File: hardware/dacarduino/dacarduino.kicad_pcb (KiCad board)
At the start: 2 copper layers, 98 x 98 mm, 78 parts, among them J1 Conn_01x03_Male, J10 Conn_01x02, J11 GATE IN, J12 GATE IN, J13 GATE IN, J14 GATE IN, J15 CV IN, J16 CV IN, J17 CV IN, J18 CV IN, J2 Conn_01x03_Male, J3 Molex 2 pin, J4 Molex 2 pin, J5 Molex 2 pin, J6 Molex 2 pin, J7 VCC, J8 EURO_PWR_2x5, J9 Conn_01x04, Q1 2N3904, Q2 2N3904, Q3 2N3904, Q4 2N3904, Q5 2N3904, Q6 2N3904, U1 MCP4922, U2 TL072, U3 REF02CP+

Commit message: Added hack area
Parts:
- added REF**: SolderWirePad_1x01_Drill0.8mm, Connector_Wire:SolderWirePad_1x01_Drill0.8mm, F.Cu at (106.7, 81.3)
- added REF**: SolderWirePad_1x01_Drill0.8mm, Connector_Wire:SolderWirePad_1x01_Drill0.8mm, F.Cu at (116.8, 88.9)
- added REF**: SolderWirePad_1x01_Drill0.8mm, Connector_Wire:SolderWirePad_1x01_Drill0.8mm, F.Cu at (94.0, 86.4)
- added REF**: SolderWirePad_1x01_Drill0.8mm, Connector_Wire:SolderWirePad_1x01_Drill0.8mm, F.Cu at (116.8, 101.6)
- added REF**: SolderWirePad_1x01_Drill0.8mm, Connector_Wire:SolderWirePad_1x01_Drill0.8mm, F.Cu at (116.8, 91.4)
- added REF**: SolderWirePad_1x01_Drill0.8mm, Connector_Wire:SolderWirePad_1x01_Drill0.8mm, F.Cu at (116.8, 99.1)
- added REF**: SolderWirePad_1x01_Drill0.8mm, Connector_Wire:SolderWirePad_1x01_Drill0.8mm, F.Cu at (116.8, 94.0)
- added REF**: SolderWirePad_1x01_Drill0.8mm, Connector_Wire:SolderWirePad_1x01_Drill0.8mm, F.Cu at (116.8, 96.5)
- added REF**: SolderWirePad_1x01_Drill0.8mm, Connector_Wire:SolderWirePad_1x01_Drill0.8mm, F.Cu at (101.6, 78.7)
- added REF**: SolderWirePad_1x01_Drill0.8mm, Connector_Wire:SolderWirePad_1x01_Drill0.8mm, F.Cu at (101.6, 81.3)
- added REF**: SolderWirePad_1x01_Drill0.8mm, Connector_Wire:SolderWirePad_1x01_Drill0.8mm, F.Cu at (101.6, 83.8)
- added REF**: SolderWirePad_1x01_Drill0.8mm, Connector_Wire:SolderWirePad_1x01_Drill0.8mm, F.Cu at (91.4, 78.7)
- added REF**: SolderWirePad_1x01_Drill0.8mm, Connector_Wire:SolderWirePad_1x01_Drill0.8mm, F.Cu at (104.1, 81.3)
- added REF**: SolderWirePad_1x01_Drill0.8mm, Connector_Wire:SolderWirePad_1x01_Drill0.8mm, F.Cu at (96.5, 78.7)
- added REF**: SolderWirePad_1x01_Drill0.8mm, Connector_Wire:SolderWirePad_1x01_Drill0.8mm, F.Cu at (99.1, 78.7)
- added REF**: SolderWirePad_1x01_Drill0.8mm, Connector_Wire:SolderWirePad_1x01_Drill0.8mm, F.Cu at (94.0, 78.7)
- added REF**: SolderWirePad_1x01_Drill0.8mm, Connector_Wire:SolderWirePad_1x01_Drill0.8mm, F.Cu at (91.4, 81.3)
- added REF**: SolderWirePad_1x01_Drill0.8mm, Connector_Wire:SolderWirePad_1x01_Drill0.8mm, F.Cu at (96.5, 81.3)
- added REF**: SolderWirePad_1x01_Drill0.8mm, Connector_Wire:SolderWirePad_1x01_Drill0.8mm, F.Cu at (94.0, 81.3)
- added REF**: SolderWirePad_1x01_Drill0.8mm, Connector_Wire:SolderWirePad_1x01_Drill0.8mm, F.Cu at (99.1, 81.3)
- added REF**: SolderWirePad_1x01_Drill0.8mm, Connector_Wire:SolderWirePad_1x01_Drill0.8mm, F.Cu at (94.0, 83.8)
- added REF**: SolderWirePad_1x01_Drill0.8mm, Connector_Wire:SolderWirePad_1x01_Drill0.8mm, F.Cu at (99.1, 83.8)
- added REF**: SolderWirePad_1x01_Drill0.8mm, Connector_Wire:SolderWirePad_1x01_Drill0.8mm, F.Cu at (96.5, 83.8)
- added REF**: SolderWirePad_1x01_Drill0.8mm, Connector_Wire:SolderWirePad_1x01_Drill0.8mm, F.Cu at (104.1, 83.8)
- added REF**: SolderWirePad_1x01_Drill0.8mm, Connector_Wire:SolderWirePad_1x01_Drill0.8mm, F.Cu at (91.4, 83.8)
- added REF**: SolderWirePad_1x01_Drill0.8mm, Connector_Wire:SolderWirePad_1x01_Drill0.8mm, F.Cu at (114.3, 99.1)
- added REF**: SolderWirePad_1x01_Drill0.8mm, Connector_Wire:SolderWirePad_1x01_Drill0.8mm, F.Cu at (114.3, 101.6)
- added REF**: SolderWirePad_1x01_Drill0.8mm, Connector_Wire:SolderWirePad_1x01_Drill0.8mm, F.Cu at (114.3, 94.0)
- added REF**: SolderWirePad_1x01_Drill0.8mm, Connector_Wire:SolderWirePad_1x01_Drill0.8mm, F.Cu at (114.3, 96.5)
- added REF**: SolderWirePad_1x01_Drill0.8mm, Connector_Wire:SolderWirePad_1x01_Drill0.8mm, F.Cu at (114.3, 91.4)
- added REF**: SolderWirePad_1x01_Drill0.8mm, Connector_Wire:SolderWirePad_1x01_Drill0.8mm, F.Cu at (114.3, 88.9)
- added REF**: SolderWirePad_1x01_Drill0.8mm, Connector_Wire:SolderWirePad_1x01_Drill0.8mm, F.Cu at (101.6, 104.1)
- added REF**: SolderWirePad_1x01_Drill0.8mm, Connector_Wire:SolderWirePad_1x01_Drill0.8mm, F.Cu at (104.1, 104.1)
- added REF**: SolderWirePad_1x01_Drill0.8mm, Connector_Wire:SolderWirePad_1x01_Drill0.8mm, F.Cu at (99.1, 104.1)
- added REF**: SolderWirePad_1x01_Drill0.8mm, Connector_Wire:SolderWirePad_1x01_Drill0.8mm, F.Cu at (106.7, 83.8)
- added REF**: SolderWirePad_1x01_Drill0.8mm, Connector_Wire:SolderWirePad_1x01_Drill0.8mm, F.Cu at (91.4, 104.1)
- added REF**: SolderWirePad_1x01_Drill0.8mm, Connector_Wire:SolderWirePad_1x01_Drill0.8mm, F.Cu at (94.0, 104.1)
- added REF**: SolderWirePad_1x01_Drill0.8mm, Connector_Wire:SolderWirePad_1x01_Drill0.8mm, F.Cu at (106.7, 104.1)
- added REF**: SolderWirePad_1x01_Drill0.8mm, Connector_Wire:SolderWirePad_1x01_Drill0.8mm, F.Cu at (109.2, 104.1)
- added REF**: SolderWirePad_1x01_Drill0.8mm, Connector_Wire:SolderWirePad_1x01_Drill0.8mm, F.Cu at (96.5, 104.1)
- added REF**: SolderWirePad_1x01_Drill0.8mm, Connector_Wire:SolderWirePad_1x01_Drill0.8mm, F.Cu at (99.1, 101.6)
- added REF**: SolderWirePad_1x01_Drill0.8mm, Connector_Wire:SolderWirePad_1x01_Drill0.8mm, F.Cu at (104.1, 101.6)
- added REF**: SolderWirePad_1x01_Drill0.8mm, Connector_Wire:SolderWirePad_1x01_Drill0.8mm, F.Cu at (91.4, 101.6)
- added REF**: SolderWirePad_1x01_Drill0.8mm, Connector_Wire:SolderWirePad_1x01_Drill0.8mm, F.Cu at (106.7, 101.6)
- added REF**: SolderWirePad_1x01_Drill0.8mm, Connector_Wire:SolderWirePad_1x01_Drill0.8mm, F.Cu at (109.2, 101.6)
- added REF**: SolderWirePad_1x01_Drill0.8mm, Connector_Wire:SolderWirePad_1x01_Drill0.8mm, F.Cu at (109.2, 83.8)
- added REF**: SolderWirePad_1x01_Drill0.8mm, Connector_Wire:SolderWirePad_1x01_Drill0.8mm, F.Cu at (96.5, 101.6)
- added REF**: SolderWirePad_1x01_Drill0.8mm, Connector_Wire:SolderWirePad_1x01_Drill0.8mm, F.Cu at (94.0, 101.6)
- added REF**: SolderWirePad_1x01_Drill0.8mm, Connector_Wire:SolderWirePad_1x01_Drill0.8mm, F.Cu at (101.6, 101.6)
- added REF**: SolderWirePad_1x01_Drill0.8mm, Connector_Wire:SolderWirePad_1x01_Drill0.8mm, F.Cu at (104.1, 99.1)
- added REF**: SolderWirePad_1x01_Drill0.8mm, Connector_Wire:SolderWirePad_1x01_Drill0.8mm, F.Cu at (106.7, 99.1)
- added REF**: SolderWirePad_1x01_Drill0.8mm, Connector_Wire:SolderWirePad_1x01_Drill0.8mm, F.Cu at (94.0, 99.1)
- added REF**: SolderWirePad_1x01_Drill0.8mm, Connector_Wire:SolderWirePad_1x01_Drill0.8mm, F.Cu at (91.4, 99.1)
- added REF**: SolderWirePad_1x01_Drill0.8mm, Connector_Wire:SolderWirePad_1x01_Drill0.8mm, F.Cu at (101.6, 99.1)
- added REF**: SolderWirePad_1x01_Drill0.8mm, Connector_Wire:SolderWirePad_1x01_Drill0.8mm, F.Cu at (99.1, 99.1)
- added REF**: SolderWirePad_1x01_Drill0.8mm, Connector_Wire:SolderWirePad_1x01_Drill0.8mm, F.Cu at (96.5, 99.1)
- added REF**: SolderWirePad_1x01_Drill0.8mm, Connector_Wire:SolderWirePad_1x01_Drill0.8mm, F.Cu at (109.2, 81.3)
- added REF**: SolderWirePad_1x01_Drill0.8mm, Connector_Wire:SolderWirePad_1x01_Drill0.8mm, F.Cu at (109.2, 99.1)
- added REF**: SolderWirePad_1x01_Drill0.8mm, Connector_Wire:SolderWirePad_1x01_Drill0.8mm, F.Cu at (101.6, 96.5)
- added REF**: SolderWirePad_1x01_Drill0.8mm, Connector_Wire:SolderWirePad_1x01_Drill0.8mm, F.Cu at (109.2, 96.5)
- added REF**: SolderWirePad_1x01_Drill0.8mm, Connector_Wire:SolderWirePad_1x01_Drill0.8mm, F.Cu at (96.5, 96.5)
- added REF**: SolderWirePad_1x01_Drill0.8mm, Connector_Wire:SolderWirePad_1x01_Drill0.8mm, F.Cu at (91.4, 96.5)
- added REF**: SolderWirePad_1x01_Drill0.8mm, Connector_Wire:SolderWirePad_1x01_Drill0.8mm, F.Cu at (104.1, 96.5)
- added REF**: SolderWirePad_1x01_Drill0.8mm, Connector_Wire:SolderWirePad_1x01_Drill0.8mm, F.Cu at (106.7, 96.5)
- added REF**: SolderWirePad_1x01_Drill0.8mm, Connector_Wire:SolderWirePad_1x01_Drill0.8mm, F.Cu at (99.1, 96.5)
- added REF**: SolderWirePad_1x01_Drill0.8mm, Connector_Wire:SolderWirePad_1x01_Drill0.8mm, F.Cu at (94.0, 96.5)
- added REF**: SolderWirePad_1x01_Drill0.8mm, Connector_Wire:SolderWirePad_1x01_Drill0.8mm, F.Cu at (94.0, 94.0)
- added REF**: SolderWirePad_1x01_Drill0.8mm, Connector_Wire:SolderWirePad_1x01_Drill0.8mm, F.Cu at (109.2, 78.7)
- added REF**: SolderWirePad_1x01_Drill0.8mm, Connector_Wire:SolderWirePad_1x01_Drill0.8mm, F.Cu at (96.5, 94.0)
- added REF**: SolderWirePad_1x01_Drill0.8mm, Connector_Wire:SolderWirePad_1x01_Drill0.8mm, F.Cu at (109.2, 94.0)
- added REF**: SolderWirePad_1x01_Drill0.8mm, Connector_Wire:SolderWirePad_1x01_Drill0.8mm, F.Cu at (101.6, 94.0)
- added REF**: SolderWirePad_1x01_Drill0.8mm, Connector_Wire:SolderWirePad_1x01_Drill0.8mm, F.Cu at (91.4, 94.0)
- added REF**: SolderWirePad_1x01_Drill0.8mm, Connector_Wire:SolderWirePad_1x01_Drill0.8mm, F.Cu at (106.7, 94.0)
- added REF**: SolderWirePad_1x01_Drill0.8mm, Connector_Wire:SolderWirePad_1x01_Drill0.8mm, F.Cu at (99.1, 94.0)
- added REF**: SolderWirePad_1x01_Drill0.8mm, Connector_Wire:SolderWirePad_1x01_Drill0.8mm, F.Cu at (104.1, 94.0)
- added REF**: SolderWirePad_1x01_Drill0.8mm, Connector_Wire:SolderWirePad_1x01_Drill0.8mm, F.Cu at (106.7, 91.4)
- added REF**: SolderWirePad_1x01_Drill0.8mm, Connector_Wire:SolderWirePad_1x01_Drill0.8mm, F.Cu at (91.4, 91.4)
- added REF**: SolderWirePad_1x01_Drill0.8mm, Connector_Wire:SolderWirePad_1x01_Drill0.8mm, F.Cu at (104.1, 91.4)
- added REF**: SolderWirePad_1x01_Drill0.8mm, Connector_Wire:SolderWirePad_1x01_Drill0.8mm, F.Cu at (106.7, 78.7)
- added REF**: SolderWirePad_1x01_Drill0.8mm, Connector_Wire:SolderWirePad_1x01_Drill0.8mm, F.Cu at (94.0, 91.4)
- added REF**: SolderWirePad_1x01_Drill0.8mm, Connector_Wire:SolderWirePad_1x01_Drill0.8mm, F.Cu at (109.2, 91.4)
- added REF**: SolderWirePad_1x01_Drill0.8mm, Connector_Wire:SolderWirePad_1x01_Drill0.8mm, F.Cu at (96.5, 91.4)
- added REF**: SolderWirePad_1x01_Drill0.8mm, Connector_Wire:SolderWirePad_1x01_Drill0.8mm, F.Cu at (99.1, 91.4)
- added REF**: SolderWirePad_1x01_Drill0.8mm, Connector_Wire:SolderWirePad_1x01_Drill0.8mm, F.Cu at (101.6, 91.4)
- added REF**: SolderWirePad_1x01_Drill0.8mm, Connector_Wire:SolderWirePad_1x01_Drill0.8mm, F.Cu at (94.0, 88.9)
- added REF**: SolderWirePad_1x01_Drill0.8mm, Connector_Wire:SolderWirePad_1x01_Drill0.8mm, F.Cu at (106.7, 88.9)
- added REF**: SolderWirePad_1x01_Drill0.8mm, Connector_Wire:SolderWirePad_1x01_Drill0.8mm, F.Cu at (99.1, 88.9)
- added REF**: SolderWirePad_1x01_Drill0.8mm, Connector_Wire:SolderWirePad_1x01_Drill0.8mm, F.Cu at (109.2, 88.9)
- added REF**: SolderWirePad_1x01_Drill0.8mm, Connector_Wire:SolderWirePad_1x01_Drill0.8mm, F.Cu at (96.5, 88.9)
- added REF**: SolderWirePad_1x01_Drill0.8mm, Connector_Wire:SolderWirePad_1x01_Drill0.8mm, F.Cu at (104.1, 78.7)
- added REF**: SolderWirePad_1x01_Drill0.8mm, Connector_Wire:SolderWirePad_1x01_Drill0.8mm, F.Cu at (101.6, 88.9)
- added REF**: SolderWirePad_1x01_Drill0.8mm, Connector_Wire:SolderWirePad_1x01_Drill0.8mm, F.Cu at (91.4, 88.9)
- added REF**: SolderWirePad_1x01_Drill0.8mm, Connector_Wire:SolderWirePad_1x01_Drill0.8mm, F.Cu at (104.1, 88.9)
- added REF**: SolderWirePad_1x01_Drill0.8mm, Connector_Wire:SolderWirePad_1x01_Drill0.8mm, F.Cu at (91.4, 86.4)
- added REF**: SolderWirePad_1x01_Drill0.8mm, Connector_Wire:SolderWirePad_1x01_Drill0.8mm, F.Cu at (109.2, 86.4)
- added REF**: SolderWirePad_1x01_Drill0.8mm, Connector_Wire:SolderWirePad_1x01_Drill0.8mm, F.Cu at (106.7, 86.4)
- added REF**: SolderWirePad_1x01_Drill0.8mm, Connector_Wire:SolderWirePad_1x01_Drill0.8mm, F.Cu at (104.1, 86.4)
- added REF**: SolderWirePad_1x01_Drill0.8mm, Connector_Wire:SolderWirePad_1x01_Drill0.8mm, F.Cu at (101.6, 86.4)
- added REF**: SolderWirePad_1x01_Drill0.8mm, Connector_Wire:SolderWirePad_1x01_Drill0.8mm, F.Cu at (99.1, 86.4)
- added REF**: SolderWirePad_1x01_Drill0.8mm, Connector_Wire:SolderWirePad_1x01_Drill0.8mm, F.Cu at (96.5, 86.4)
- moved R12 6.74 mm to (120.7, 79.4)
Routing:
- net /Arduino/DAC_CS: track 63.8 -> 60.6 mm
- net VCC: track 264.7 -> 266.1 mm
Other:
- board text added: "GND"
- board text added: "Hack me here"
- board text added: "VCC"

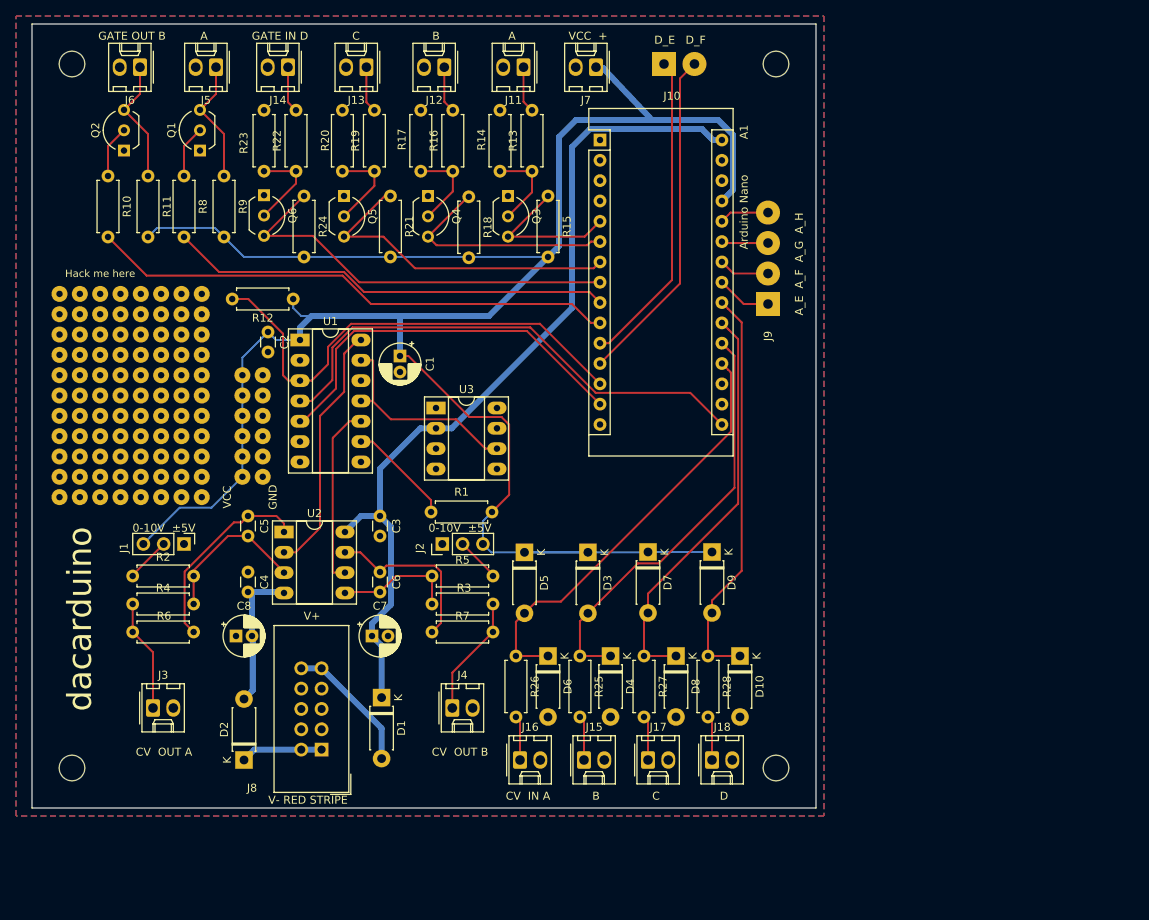
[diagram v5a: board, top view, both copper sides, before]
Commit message: Add multiplexer option
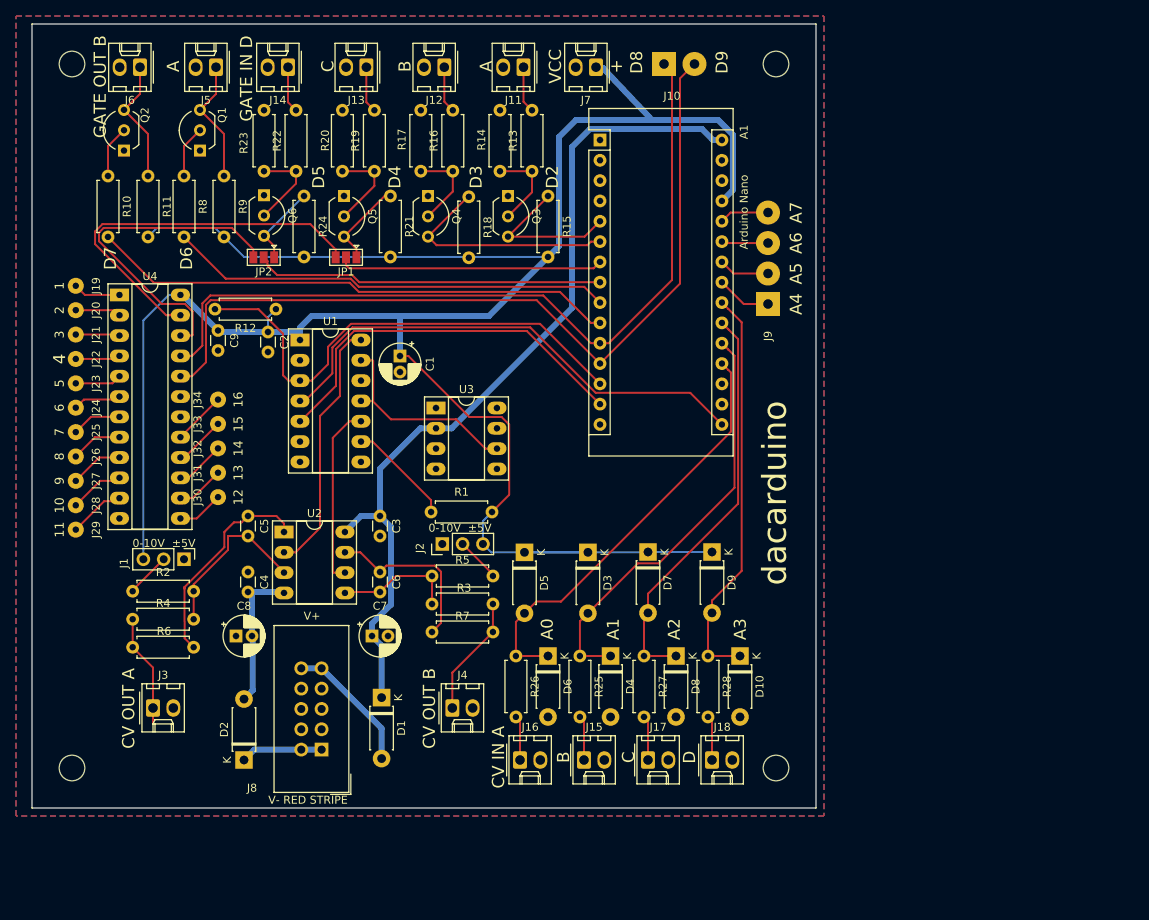
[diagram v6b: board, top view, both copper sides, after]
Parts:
- removed REF** (x100): SolderWirePad_1x01_Drill0.8mm, Connector_Wire:SolderWirePad_1x01_Drill0.8mm
- added C9: 0.1uF, Capacitor_THT:C_Disc_D3.0mm_W1.6mm_P2.50mm, F.Cu at (111.3, 83.3)
- added J19: Conn_01x01, Connector_Wire:SolderWirePad_1x01_Drill0.8mm, F.Cu at (93.5, 77.7)
- added J20: Conn_01x01, Connector_Wire:SolderWirePad_1x01_Drill0.8mm, F.Cu at (93.5, 80.8)
- added J21: Conn_01x01, Connector_Wire:SolderWirePad_1x01_Drill0.8mm, F.Cu at (93.5, 83.8)
- added J22: Conn_01x01, Connector_Wire:SolderWirePad_1x01_Drill0.8mm, F.Cu at (93.5, 86.9)
- added J23: Conn_01x01, Connector_Wire:SolderWirePad_1x01_Drill0.8mm, F.Cu at (93.5, 89.9)
- added J24: Conn_01x01, Connector_Wire:SolderWirePad_1x01_Drill0.8mm, F.Cu at (93.5, 93.0)
- added J25: Conn_01x01, Connector_Wire:SolderWirePad_1x01_Drill0.8mm, F.Cu at (93.5, 96.0)
- added J26: Conn_01x01, Connector_Wire:SolderWirePad_1x01_Drill0.8mm, F.Cu at (93.5, 99.1)
- added J27: Conn_01x01, Connector_Wire:SolderWirePad_1x01_Drill0.8mm, F.Cu at (93.5, 102.1)
- added J28: Conn_01x01, Connector_Wire:SolderWirePad_1x01_Drill0.8mm, F.Cu at (93.5, 105.2)
- added J29: Conn_01x01, Connector_Wire:SolderWirePad_1x01_Drill0.8mm, F.Cu at (93.5, 108.2)
- added J30: Conn_01x01, Connector_Wire:SolderWirePad_1x01_Drill0.8mm, F.Cu at (111.3, 104.1)
- added J31: Conn_01x01, Connector_Wire:SolderWirePad_1x01_Drill0.8mm, F.Cu at (111.3, 101.1)
- added J32: Conn_01x01, Connector_Wire:SolderWirePad_1x01_Drill0.8mm, F.Cu at (111.3, 98.0)
- added J33: Conn_01x01, Connector_Wire:SolderWirePad_1x01_Drill0.8mm, F.Cu at (111.3, 95.0)
- added J34: Conn_01x01, Connector_Wire:SolderWirePad_1x01_Drill0.8mm, F.Cu at (111.3, 91.9)
- added JP1: SolderJumper_3_Open, Jumper:SolderJumper-3_P1.3mm_Open_Pad1.0x1.5mm, F.Cu at (127.3, 74.2)
- added JP2: SolderJumper_3_Open, Jumper:SolderJumper-3_P1.3mm_Open_Pad1.0x1.5mm, F.Cu at (117.0, 74.2)
- added U4: SN74LS154N, Package_DIP:DIP-24_W7.62mm_Socket_LongPads, F.Cu at (98.9, 78.9)
- moved R12 2.50 mm to (118.5, 80.6)
- moved J1 1.91 mm to (107.0, 111.9)
- moved R2 1.91 mm to (100.6, 115.9)
- moved R4 1.91 mm to (108.2, 119.4)
- moved R6 1.91 mm to (108.2, 122.9)
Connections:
- net /Arduino/A_IN_A renamed /Arduino/A0
- net /Arduino/A_IN_B renamed /Arduino/A1
- net /Arduino/A_IN_C renamed /Arduino/A2
- net /Arduino/A_IN_D renamed /Arduino/A3
- net /Arduino/A_IN_E renamed /Arduino/A4
- net /Arduino/A_IN_F renamed /Arduino/A5
- net /Arduino/A_IN_G renamed /Arduino/A6
- net /Arduino/A_IN_H renamed /Arduino/A7
- net /Arduino/D_IN_A renamed /Arduino/D2
- net /Arduino/D_IN_B renamed /Arduino/D3
- net /Arduino/D_IN_E renamed /Arduino/D8
- net /Arduino/D_IN_F renamed /Arduino/D9
- net /Arduino/D_OUT_A renamed /Arduino/D6
- net /Arduino/D_OUT_B renamed /Arduino/D7
- A1 pad 7: /Arduino/D_IN_C -> /Arduino/D4
- A1 pad 8: /Arduino/D_IN_D -> /Arduino/D5
- Q5 pad 3: /Arduino/D_IN_C -> /Inputs/Gate in C/D_IN
- Q6 pad 3: /Arduino/D_IN_D -> /Inputs/Gate in D/D_IN
- R21 pad 1: /Arduino/D_IN_C -> /Inputs/Gate in C/D_IN
- R24 pad 1: /Arduino/D_IN_D -> /Inputs/Gate in D/D_IN
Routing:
- net /Arduino/D9: track 42.3 -> 106.2 mm
- net /Arduino/D8: track 39.7 -> 100.8 mm
- net /Arduino/D_IN_D: track 51.5 -> 0.00 mm
- net Net-(JP1-Pad3): track 0.00 -> 49.6 mm
- net /Arduino/D5: track 0.00 -> 43.6 mm
- net Net-(JP2-Pad3): track 0.00 -> 42.5 mm
- net /Arduino/D_IN_C: track 41.9 -> 0.00 mm
- net /Arduino/D4: track 0.00 -> 33.2 mm
- net VCC: track 266.1 -> 279.5 mm
- net /Inputs/Gate in C/D_IN: track 0.00 -> 11.1 mm
- net /Inputs/Gate in D/D_IN: track 0.00 -> 10.3 mm
- net Net-(J29-Pad1): track 0.00 -> 7.09 mm
- net Net-(J28-Pad1): track 0.00 -> 6.88 mm
- net Net-(J27-Pad1): track 0.00 -> 6.67 mm
- net Net-(J34-Pad1): track 0.00 -> 6.65 mm
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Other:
- board text added: "+"
- board text added: "1"
- board text added: "10"
- board text added: "11"
- board text added: "12"
- board text added: "13"
- board text added: "14"
- board text added: "15"
- board text added: "16"
- board text added: "2"
- board text added: "3"
- board text added: "4"
- board text added: "5"
- board text added: "6"
- board text added: "7"
- board text added: "8"
- board text added: "9"
- board text added: "A0"
- board text added: "A1"
- board text added: "A2"
- board text added: "A3"
- board text added: "A4"
- board text added: "A5"
- board text added: "A6"
- board text added: "A7"
- board text added: "D2"
- board text added: "D3"
- board text added: "D4"
- board text added: "D5"
- board text added: "D6"
- board text added: "D7"
- board text added: "D8"
- board text added: "D9"
- board text removed: "A_E A_F A_G A_H"
- board text removed: "D_E D_F"
- board text removed: "GND"
- board text removed: "Hack me here"
- board text removed: "VCC +"
